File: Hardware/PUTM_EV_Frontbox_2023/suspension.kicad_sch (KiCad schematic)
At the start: 0 parts

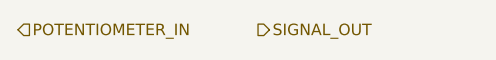
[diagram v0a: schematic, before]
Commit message: Added MCU wiring
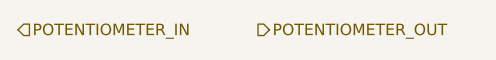
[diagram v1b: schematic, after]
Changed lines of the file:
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@@
     (effects (font (size 1.27 1.27)) (justify left))
   )
-  (hierarchical_label "SIGNAL_OUT" (shape output) (at 109.22 83.82 0) (fields_autoplaced)
+  (hierarchical_label "POTENTIOMETER_OUT" (shape output) (at 109.22 83.82 0) (fields_autoplaced)
     (effects (font (size 1.27 1.27)) (justify left))
   )

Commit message: Schematic ready for review
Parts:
- added 5k1: R_Small, symbol Device:R_Small
- added C27: 100n, symbol Device:C_Small
- added R17, R18, R19, R20, R21: 5k, symbol Device:R_Small
- added R22, R23, R26, R27: 3k, symbol Device:R_Small
- added R24, R25, R28, R29: 12k, symbol Device:R_Small
- added U2: TLV9152IDDFR, symbol Amplifier_Operational:TLV9062
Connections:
- net POTENTIOMETER_IN: now also R17.2, R22.1, R23.1
- net POTENTIOMETER_OUT: now also R28.2, U2.1
- new net: R27.2, R29.1, U2.6 (-)
- new net: R23.2, R25.2, U2.5 (+)
- new net: R22.2, R24.2, U2.3 (+)
- new net: R26.2, R28.1, U2.2 (-)
- new net +5V: C27.1, R17.1, R18.1, R19.1, R20.1, U2.8 (V+)
- new net GND: 5k1.2, C27.2, R21.2, R24.1, R25.1, U2.4 (V-)
- new net IN1-: 5k1.1, R19.2, R26.1, R27.1
- new net IN2-: R20.2, R21.1
- new net POTENTIOMETER2_OUT: R29.2, U2.7
- new net POTENTIOMETER_IN2: R18.2
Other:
- note added: "Gain subject to change to better fit actual potentiometer characteristics"

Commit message: Fixed all issues
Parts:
- removed 5k1: R_Small, symbol Device:R_Small
- removed R19: 5k, symbol Device:R_Small
- added R76, R77: 10k, symbol Device:R_Small
- R20, R21: value 5k -> 10k
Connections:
- net +5V: no longer C27.1, R20.1, U2.8 (V+)
- net GND: now also R77.2
- net POTENTIOMETER_IN: now also R26.1; no longer R22.1, R23.1
- net POTENTIOMETER_IN2: now also R27.1
- removed net IN1-: R26.1, R27.1
- net IN2- renamed IN1+
- net IN1+: now also R22.1
- new net +3.3V: C27.1, U2.8 (V+)
- new net 5v_ref: R20.1, R76.1
- new net IN2+: R23.1, R76.2, R77.1

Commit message: Schematic modified, footprints assigned
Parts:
- C27: footprint (none) -> Capacitor_SMD:C_0402_1005Metric_Pad0.74x0.62mm_HandSolder
- R17, R18, R20, R21, R22, R23, R24, R25, R26, R27, R28, R29, R76, R77: footprint (none) -> Resistor_SMD:R_0402_1005Metric
- U2: footprint (none) -> Package_TO_SOT_SMD:TSOT-23-8_HandSoldering
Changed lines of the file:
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@@
       (effects (font (size 1.27 1.27)) (justify left))
     )
-    (property "Footprint" "" (at 104.775 85.09 0)
+    (property "Footprint" "Resistor_SMD:R_0402_1005Metric" (at 104.775 85.09 0)
       (effects (font (size 1.27 1.27)) hide)
     )
@@
       (effects (font (size 1.27 1.27)))
     )
-    (property "Footprint" "" (at 160.655 127 0)
+    (property "Footprint" "Resistor_SMD:R_0402_1005Metric" (at 160.655 127 0)
       (effects (font (size 1.27 1.27)) hide)
     )
@@
       (effects (font (size 1.27 1.27)) (justify left))
     )
-    (property "Footprint" "" (at 95.25 115.57 0)
+    (property "Footprint" "Resistor_SMD:R_0402_1005Metric" (at 95.25 115.57 0)
       (effects (font (size 1.27 1.27)) hide)
     )
@@
       (effects (font (size 1.27 1.27)))
     )
-    (property "Footprint" "" (at 161.925 118.11 0)
+    (property "Footprint" "Package_TO_SOT_SMD:TSOT-23-8_HandSoldering" (at 161.925 118.11 0)
       (effects (font (size 1.27 1.27)) hide)
     )
@@
       (effects (font (size 1.27 1.27)) (justify left))
     )
-    (property "Footprint" "" (at 214.63 97.79 0)
+    (property "Footprint" "Package_TO_SOT_SMD:TSOT-23-8_HandSoldering" (at 214.63 97.79 0)
       (effects (font (size 1.27 1.27)) hide)
     )
@@
       (effects (font (size 1.27 1.27)))
     )
-    (property "Footprint" "" (at 128.905 76.2 0)
+    (property "Footprint" "Resistor_SMD:R_0402_1005Metric" (at 128.905 76.2 0)
       (effects (font (size 1.27 1.27)) hide)
     )
@@
       (effects (font (size 1.27 1.27)))
     )
-    (property "Footprint" "" (at 147.955 81.28 0)
+    (property "Footprint" "Resistor_SMD:R_0402_1005Metric" (at 147.955 81.28 0)
       (effects (font (size 1.27 1.27)) hide)
     )
@@
       (effects (font (size 1.27 1.27)) (justify left))
     )
-    (property "Footprint" "" (at 207.01 97.79 0)
+    (property "Footprint" "Capacitor_SMD:C_0402_1005Metric_Pad0.74x0.62mm_HandSolder" (at 207.01 97.79 0)
       (effects (font (size 1.27 1.27)) hide)
     )
@@
       (effects (font (size 1.27 1.27)))
     )
-    (property "Footprint" "" (at 160.655 87.63 0)
+    (property "Footprint" "Resistor_SMD:R_0402_1005Metric" (at 160.655 87.63 0)
       (effects (font (size 1.27 1.27)) hide)
     )
@@
       (effects (font (size 1.27 1.27)) (justify left))
     )
-    (property "Footprint" "" (at 104.775 126.365 0)
+    (property "Footprint" "Resistor_SMD:R_0402_1005Metric" (at 104.775 126.365 0)
       (effects (font (size 1.27 1.27)) hide)
     )
@@
       (effects (font (size 1.27 1.27)) (justify left))
     )
-    (property "Footprint" "" (at 95.25 74.295 0)
+    (property "Footprint" "Resistor_SMD:R_0402_1005Metric" (at 95.25 74.295 0)
       (effects (font (size 1.27 1.27)) hide)
     )
@@
       (effects (font (size 1.27 1.27)) (justify left))
     )
-    (property "Footprint" "" (at 104.775 115.57 0)
+    (property "Footprint" "Resistor_SMD:R_0402_1005Metric" (at 104.775 115.57 0)
       (effects (font (size 1.27 1.27)) hide)
     )
@@
       (effects (font (size 1.27 1.27)))
     )
-    (property "Footprint" "" (at 128.905 115.57 0)
+    (property "Footprint" "Resistor_SMD:R_0402_1005Metric" (at 128.905 115.57 0)
       (effects (font (size 1.27 1.27)) hide)
     )
@@
       (effects (font (size 1.27 1.27)) (justify right))
     )
-    (property "Footprint" "" (at 135.255 119.38 0)
+    (property "Footprint" "Resistor_SMD:R_0402_1005Metric" (at 135.255 119.38 0)
       (effects (font (size 1.27 1.27)) hide)
     )
@@
       (effects (font (size 1.27 1.27)) (justify right))
     )
-    (property "Footprint" "" (at 135.255 80.01 0)
+    (property "Footprint" "Resistor_SMD:R_0402_1005Metric" (at 135.255 80.01 0)
       (effects (font (size 1.27 1.27)) hide)
     )
@@
       (effects (font (size 1.27 1.27)))
     )
-    (property "Footprint" "" (at 147.955 120.65 0)
+    (property "Footprint" "Resistor_SMD:R_0402_1005Metric" (at 147.955 120.65 0)
       (effects (font (size 1.27 1.27)) hide)
     )
@@
       (effects (font (size 1.27 1.27)) (justify left))
     )
-    (property "Footprint" "" (at 104.775 74.295 0)
+    (property "Footprint" "Resistor_SMD:R_0402_1005Metric" (at 104.775 74.295 0)
       (effects (font (size 1.27 1.27)) hide)
     )
@@
       (effects (font (size 1.27 1.27)))
     )
-    (property "Footprint" "" (at 161.925 78.74 0)
-      (effects (font (size 1.27 1.27)) hide)
-    )
+    (property "Footprint" "Package_TO_SOT_SMD:TSOT-23-8_HandSoldering" (at 161.925 78.74 0)
+      (effects (font (size 1.27 1.27)) hide)
+    )

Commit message: Merged branch new_apps
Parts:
- renumbered C27 to C25, U2 to U12
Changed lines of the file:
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@@
   (symbol (lib_id "Amplifier_Operational:TLV9062") (at 161.925 118.11 0) (unit 2)
     (in_bom yes) (on_board yes) (dnp no) (fields_autoplaced)
-    (property "Reference" "U2" (at 161.925 109.22 0)
+    (property "Reference" "U12" (at 161.925 109.22 0)
       (effects (font (size 1.27 1.27)))
     )
@@
   (symbol (lib_id "Amplifier_Operational:TLV9062") (at 214.63 97.79 0) (unit 3)
     (in_bom yes) (on_board yes) (dnp no) (fields_autoplaced)
-    (property "Reference" "U2" (at 213.36 97.155 0)
+    (property "Reference" "U12" (at 213.36 97.155 0)
       (effects (font (size 1.27 1.27)) (justify left))
     )
@@
   (symbol (lib_id "Device:C_Small") (at 207.01 97.79 0) (mirror y) (unit 1)
     (in_bom yes) (on_board yes) (dnp no)
-    (property "Reference" "C27" (at 204.47 97.155 0)
+    (property "Reference" "C25" (at 204.47 97.155 0)
       (effects (font (size 1.27 1.27)) (justify left))
     )
@@
   (symbol (lib_id "power:GND") (at 212.09 107.95 0) (unit 1)
     (in_bom yes) (on_board yes) (dnp no) (fields_autoplaced)
-    (property "Reference" "#PWR077" (at 212.09 114.3 0)
+    (property "Reference" "#PWR091" (at 212.09 114.3 0)
       (effects (font (size 1.27 1.27)) hide)
     )
@@
   (symbol (lib_id "Amplifier_Operational:TLV9062") (at 161.925 78.74 0) (unit 1)
     (in_bom yes) (on_board yes) (dnp no) (fields_autoplaced)
-    (property "Reference" "U2" (at 161.925 69.85 0)
-      (effects (font (size 1.27 1.27)))
-    )
+    (property "Reference" "U12" (at 161.925 69.85 0)
+      (effects (font (size 1.27 1.27)))
+    )
